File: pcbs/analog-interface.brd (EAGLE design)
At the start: 76.9 x 13.5 mm, 27 parts, among them U1 ISL3179EIBZ, U2 ATMEGA328P

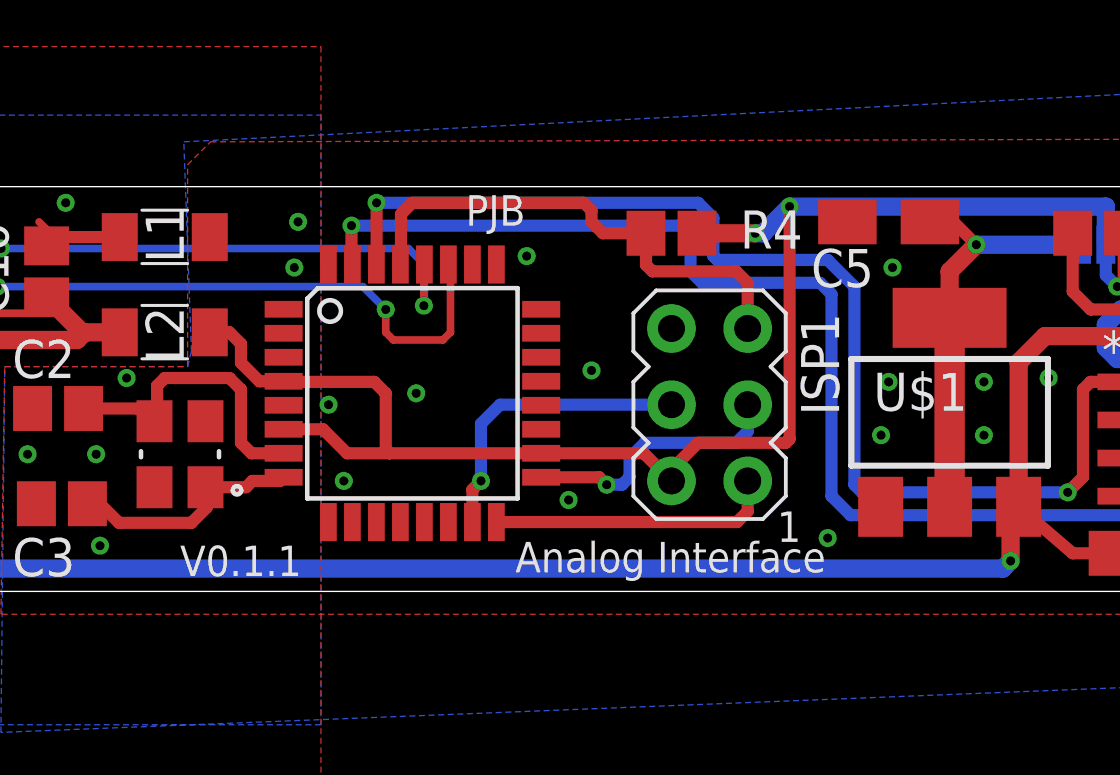
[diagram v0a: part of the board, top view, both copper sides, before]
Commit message: Pull ups added to I2C
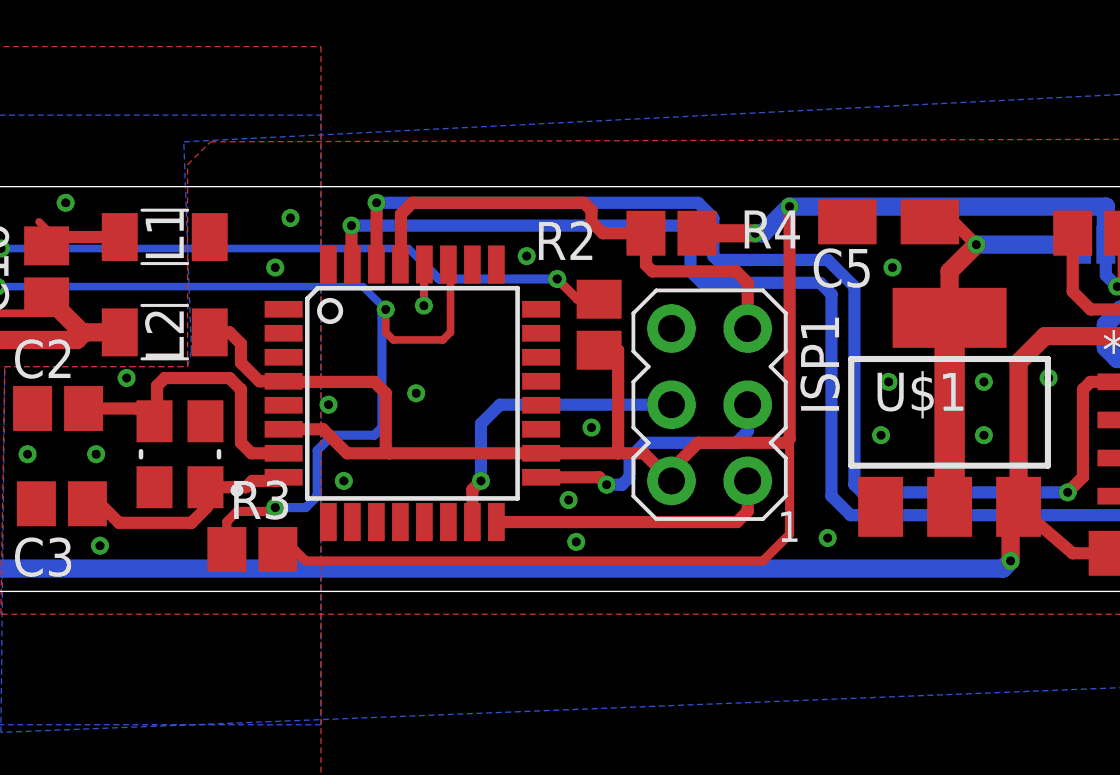
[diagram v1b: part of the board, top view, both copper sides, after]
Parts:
- added R2, R3: 1k, resistor:R0805
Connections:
- net SCL: now also R2.1
- net SDA: now also R3.1
- net VCC: now also R2.2, R3.2
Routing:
- net VCC: track 63.5 -> 88.3 mm
- net SDA: track 21.1 -> 33.3 mm, vias 2 -> 3
- net SCL: track 19.3 -> 25.6 mm, vias 2 -> 3
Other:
- board text removed: "Analog Interface"
- board text removed: "PJB"
- board text removed: "V0.1.1"
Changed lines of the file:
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@@
 <wire x1="-34.036" y1="14" x2="-34.036" y2="0.508" width="0" layer="20"/>
 <text x="35.306" y="11.684" size="1.778" layer="25">1</text>
-<text x="8.255" y="1.143" size="1.016" layer="25">Analog Interface</text>
-<text x="-2.921" y="1.016" size="1.016" layer="25">V0.1.1</text>
-<text x="6.604" y="12.7" size="1.016" layer="25">PJB</text>
 </plain>
 <attributes>
@@
 <attribute name="VALUE" x="35.179" y="13.716" size="1.27" layer="27" rot="R270"/>
 </element>
+<element name="R2" library="resistor" package="R0805" value="1k" x="11.049" y="9.398" smashed="yes" rot="R270">
+<attribute name="NAME" x="8.89" y="11.557" size="1.27" layer="25"/>
+</element>
+<element name="R3" library="resistor" package="R0805" value="1k" x="-0.508" y="1.905" smashed="yes">
+<attribute name="NAME" x="-1.27" y="2.921" size="1.27" layer="25"/>
+</element>
 </elements>
 <signals>
@@
 <via x="2.032" y="6.731" extent="1-16" drill="0.3" shape="square"/>
 <via x="2.54" y="4.191" extent="1-16" drill="0.3" shape="square"/>
-<via x="10.795" y="7.874" extent="1-16" drill="0.3" shape="square"/>
+<via x="10.795" y="5.969" extent="1-16" drill="0.3" shape="square"/>
 <via x="8.636" y="11.684" extent="1-16" drill="0.3" shape="square"/>
-<via x="1.016" y="12.827" extent="1-16" drill="0.3" shape="square"/>
-<via x="0.889" y="11.303" extent="1-16" drill="0.3" shape="square"/>
+<via x="10.287" y="2.159" extent="1-16" drill="0.3" shape="square"/>
+<via x="0.254" y="11.303" extent="1-16" drill="0.3" shape="square"/>
+<via x="0.762" y="12.954" extent="1-16" drill="0.3" shape="square"/>
 </signal>
 <signal name="VCC">
@@
 <wire x1="4.064" y1="5.112" x2="2.648" y2="5.112" width="0.4064" layer="1"/>
 <wire x1="2.648" y1="5.112" x2="1.848" y2="5.912" width="0.4064" layer="1"/>
-<wire x1="9.1186" y1="5.112" x2="12.541" y2="5.112" width="0.4064" layer="1"/>
+<wire x1="9.1186" y1="5.112" x2="11.684" y2="5.112" width="0.4064" layer="1"/>
+<wire x1="11.684" y1="5.112" x2="12.541" y2="5.112" width="0.4064" layer="1"/>
 <wire x1="12.541" y1="5.112" x2="13.462" y2="4.191" width="0.4064" layer="1"/>
 <wire x1="14.312" y1="12.446" x2="16.256" y2="12.446" width="0.6096" layer="1"/>
@@
 <wire x1="3.937" y1="7.112" x2="3.937" y2="5.239" width="0.4064" layer="1"/>
 <wire x1="3.937" y1="5.239" x2="4.064" y2="5.112" width="0.4064" layer="1"/>
+<contactref element="R2" pad="2"/>
+<contactref element="R3" pad="2"/>
+<wire x1="11.049" y1="8.548" x2="11.684" y2="8.548" width="0.4064" layer="1"/>
+<wire x1="11.684" y1="8.548" x2="11.684" y2="5.112" width="0.4064" layer="1"/>
+<wire x1="17.399" y1="2.413" x2="17.399" y2="5.334" width="0.3048" layer="1"/>
+<wire x1="17.399" y1="5.334" x2="17.272" y2="5.461" width="0.3048" layer="1"/>
+<wire x1="0.342" y1="1.905" x2="0.889" y2="1.905" width="0.3048" layer="1"/>
+<wire x1="0.889" y1="1.905" x2="1.27" y2="1.524" width="0.3048" layer="1"/>
+<wire x1="1.27" y1="1.524" x2="16.51" y2="1.524" width="0.3048" layer="1"/>
+<wire x1="16.51" y1="1.524" x2="17.399" y2="2.413" width="0.3048" layer="1"/>
 </signal>
 <signal name="485_P" class="1">
@@
 <wire x1="5.207" y1="10.033" x2="5.207" y2="11.3856" width="0.254" layer="1"/>
 <wire x1="5.207" y1="11.3856" x2="5.226" y2="11.4046" width="0.254" layer="1"/>
+<contactref element="R2" pad="1"/>
+<wire x1="11.049" y1="10.248" x2="10.326" y2="10.248" width="0.3048" layer="1"/>
+<wire x1="10.326" y1="10.248" x2="9.652" y2="10.922" width="0.3048" layer="1"/>
+<via x="9.652" y="10.922" extent="1-16" drill="0.3048"/>
+<wire x1="9.652" y1="10.922" x2="5.7086" y2="10.922" width="0.3048" layer="16"/>
+<wire x1="5.7086" y1="10.922" x2="5.226" y2="11.4046" width="0.3048" layer="16"/>
 </signal>
 <signal name="SDA">
@@
 <wire x1="4.191" y1="8.89" x2="5.842" y2="8.89" width="0.254" layer="1"/>
 <wire x1="5.842" y1="8.89" x2="6.096" y2="9.144" width="0.254" layer="1"/>
+<contactref element="R3" pad="1"/>
+<wire x1="-1.358" y1="1.905" x2="-1.358" y2="2.833" width="0.3048" layer="1"/>
+<wire x1="-1.358" y1="2.833" x2="-1.016" y2="3.175" width="0.3048" layer="1"/>
+<wire x1="-1.016" y1="3.175" x2="0.127" y2="3.175" width="0.3048" layer="1"/>
+<wire x1="0.127" y1="3.175" x2="0.254" y2="3.302" width="0.3048" layer="1"/>
+<via x="0.254" y="3.302" extent="1-16" drill="0.3048"/>
+<wire x1="0.254" y1="3.302" x2="1.27" y2="3.302" width="0.3048" layer="16"/>
+<wire x1="1.27" y1="3.302" x2="1.651" y2="3.683" width="0.3048" layer="16"/>
+<wire x1="1.651" y1="3.683" x2="1.651" y2="5.207" width="0.3048" layer="16"/>
+<wire x1="1.651" y1="5.207" x2="2.159" y2="5.715" width="0.3048" layer="16"/>
+<wire x1="2.159" y1="5.715" x2="3.556" y2="5.715" width="0.3048" layer="16"/>
+<wire x1="3.556" y1="5.715" x2="3.81" y2="5.969" width="0.3048" layer="16"/>
+<wire x1="3.81" y1="5.969" x2="3.81" y2="9.779" width="0.3048" layer="16"/>
+<wire x1="3.81" y1="9.779" x2="3.937" y2="9.906" width="0.3048" layer="16"/>
 </signal>
 <signal name="ADC3">
